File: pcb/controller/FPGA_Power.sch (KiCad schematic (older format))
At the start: 25 parts

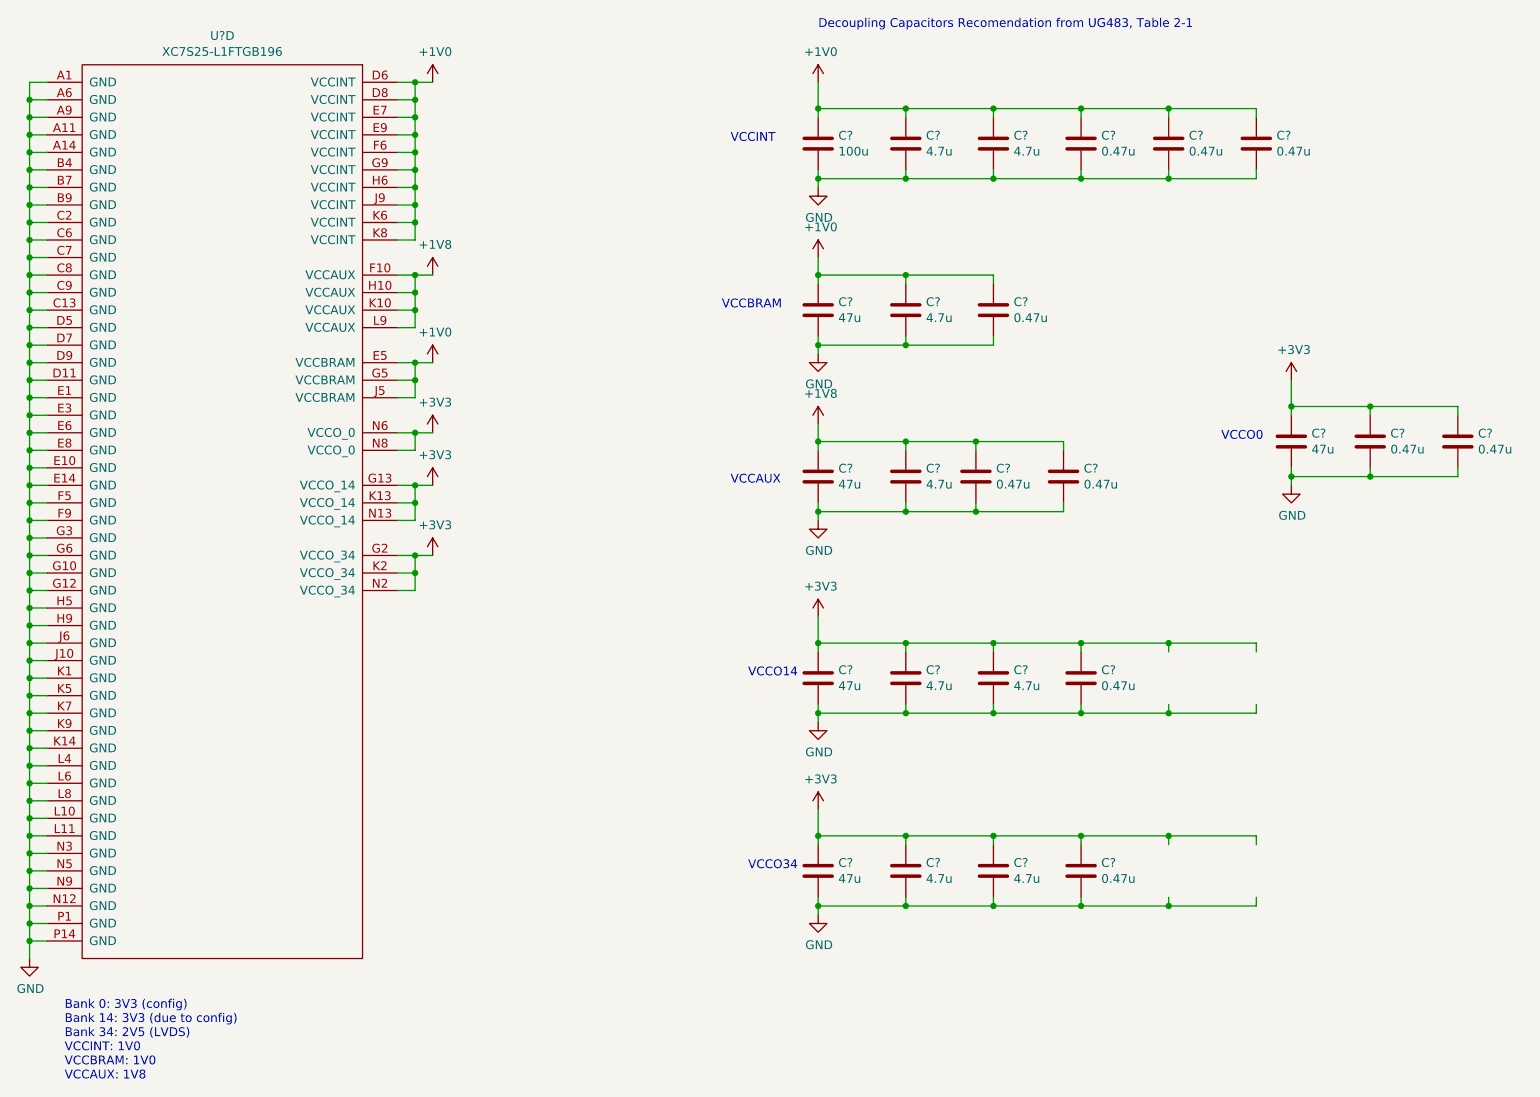
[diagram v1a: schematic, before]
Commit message: started assigning footprints
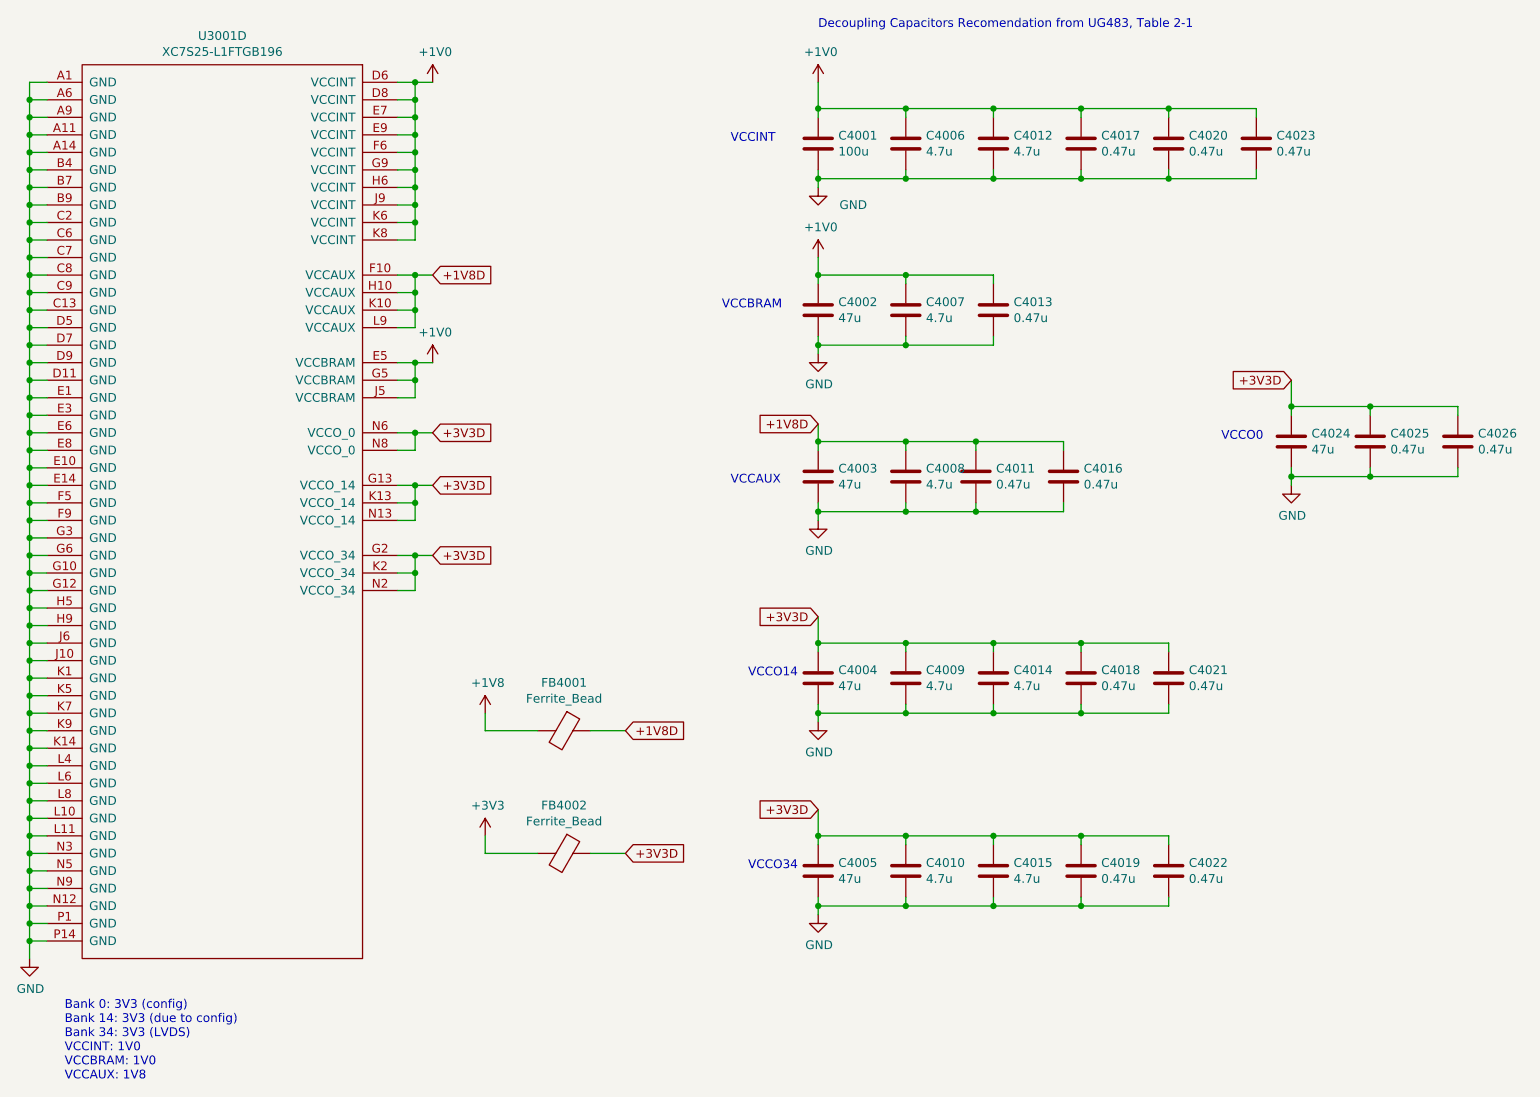
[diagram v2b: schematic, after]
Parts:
- added C4021, C4022: 0.47u, Capacitor_SMD:C_0402_1005Metric, symbol Device:C
- added FB4001, FB4002: Ferrite_Bead, symbol Device:Ferrite_Bead
- gave numbers to parts that had none: 25
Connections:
- net labels added: +1V8D, +3V3D
- wire segments 262 -> 260
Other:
- note added: "Bank 0: 3V3 (config)\nBank 14: 3V3 (due to config)\nBank 34: 3V3 (LVDS)\nVCCINT: 1V0\nVCCBRAM: 1V0\nVCCAUX: 1V8"
- note removed: "Bank 0: 3V3 (config)\nBank 14: 3V3 (due to config)\nBank 34: 2V5 (LVDS)\nVCCINT: 1V0\nVCCBRAM: 1V0\nVCCAUX: 1V8"

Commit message: pcb component placement almost done
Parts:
- removed C4005: 47u, Capacitor_SMD:C_0805_2012Metric, symbol Device:C
- FB4001, FB4002: footprint (none) -> Inductor_SMD:L_0805_2012Metric
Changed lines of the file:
@@
-$EndComp
-$Comp
-L Device:C C4005
-U 1 1 5C2F58D1
-P 6600 5700
-F 0 "C4005" H 6715 5746 50  0000 L CNN
-F 1 "47u" H 6715 5655 50  0000 L CNN
-F 2 "Capacitor_SMD:C_0805_2012Metric" H 6638 5550 50  0001 C CNN
-F 3 "~" H 6600 5700 50  0001 C CNN
-	1    6600 5700
-	1    0    0    -1
 $EndComp
 $Comp
@@
 F 0 "FB4001" V 4876 4900 50  0000 C CNN
 F 1 "Ferrite_Bead" V 4967 4900 50  0000 C CNN
-F 2 "" V 5080 4900 50  0001 C CNN
+F 2 "Inductor_SMD:L_0805_2012Metric" V 5080 4900 50  0001 C CNN
 F 3 "~" H 5150 4900 50  0001 C CNN
 	1    5150 4900
@@
 F 0 "FB4002" V 4876 5600 50  0000 C CNN
 F 1 "Ferrite_Bead" V 4967 5600 50  0000 C CNN
-F 2 "" V 5080 5600 50  0001 C CNN
+F 2 "Inductor_SMD:L_0805_2012Metric" V 5080 5600 50  0001 C CNN
 F 3 "~" H 5150 5600 50  0001 C CNN
 	1    5150 5600
